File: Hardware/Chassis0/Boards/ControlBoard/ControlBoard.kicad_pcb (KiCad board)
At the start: 6 copper layers, 297.5 x 60 mm, 138 parts, among them IC3 MAX22530AWE+, IC4 MAX22530AWE+, J1 TBP02R2W-381-06BE, J11 Conn_02x10_Counter_Clockwise, J12 Conn_02x10_Counter_Clockwise, J13 Conn_02x10_Counter_Clockwise, J14 Conn_02x10_Counter_Clockwise, J2 TBP02R2W-381-06BE, J29 Conn_01x02_Pin, J3 TBP01R2W-508-02BE, J4 TBP01R1-508-04BE, J5 Conn_02x10_Counter_Clockwise, J7 TBP02R2W-381-08BE, J8 TBP02R2W-381-08BE

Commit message: Update size 0 cad model
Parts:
- removed G***: LOGO, InverterCom:HIGHVOLTAGE_20mm
- removed J11, J12, J13, J14: Conn_02x10_Counter_Clockwise, Connector_PinSocket_2.54mm:PinSocket_2x10_P2.54mm_Vertical
- removed J4: TBP01R1-508-04BE, InverterCom:TBP01R150804BE
- added C1: 100nF, Capacitor_SMD:C_1210_3225Metric_Pad1.33x2.70mm_HandSolder, F.Cu at (14.9, -37.0)
- added C10: 100nF, Capacitor_SMD:C_1210_3225Metric_Pad1.33x2.70mm_HandSolder, F.Cu at (27.0, -32.8)
- added C100: 100nF, Capacitor_SMD:C_1210_3225Metric_Pad1.33x2.70mm_HandSolder, F.Cu at (-106.3, 55.9)
- added C101: 10uF, Capacitor_SMD:C_1210_3225Metric_Pad1.33x2.70mm_HandSolder, F.Cu at (-100.3, 43.1)
- added C102: 10uF, Capacitor_SMD:C_1210_3225Metric_Pad1.33x2.70mm_HandSolder, F.Cu at (-100.3, 47.4)
- added C103: 100nF, Capacitor_SMD:C_1210_3225Metric_Pad1.33x2.70mm_HandSolder, F.Cu at (-100.3, 51.6)
- added C104: 10uF, Capacitor_SMD:C_1210_3225Metric_Pad1.33x2.70mm_HandSolder, F.Cu at (-100.3, 55.9)
- added C105: 10uF, Capacitor_SMD:C_1210_3225Metric_Pad1.33x2.70mm_HandSolder, F.Cu at (-94.3, 43.1)
- added C106: 100nF, Capacitor_SMD:C_1210_3225Metric_Pad1.33x2.70mm_HandSolder, F.Cu at (-94.3, 47.4)
- added C107: 10uF, Capacitor_SMD:C_1210_3225Metric_Pad1.33x2.70mm_HandSolder, F.Cu at (-94.3, 51.6)
- added C108: 10nF, Capacitor_SMD:C_1210_3225Metric_Pad1.33x2.70mm_HandSolder, F.Cu at (-80.3, 74.7)
- added C109: 10nF, Capacitor_SMD:C_1210_3225Metric_Pad1.33x2.70mm_HandSolder, F.Cu at (-66.2, 74.7)
- added C11: 1uF, Capacitor_SMD:C_1210_3225Metric_Pad1.33x2.70mm_HandSolder, F.Cu at (27.0, -28.5)
- added C110: 10nF, Capacitor_SMD:C_1210_3225Metric_Pad1.33x2.70mm_HandSolder, F.Cu at (-80.3, 47.5)
- added C111: 10nF, Capacitor_SMD:C_1210_3225Metric_Pad1.33x2.70mm_HandSolder, F.Cu at (-66.2, 47.5)
- added C12: 1uF, Capacitor_SMD:C_1210_3225Metric_Pad1.33x2.70mm_HandSolder, F.Cu at (27.0, -24.2)
- added C124: 10nF, Capacitor_SMD:C_1210_3225Metric_Pad1.33x2.70mm_HandSolder, F.Cu at (-107.3, 88.4)
- added C125: 10nF, Capacitor_SMD:C_1210_3225Metric_Pad1.33x2.70mm_HandSolder, F.Cu at (-148.5, 88.4)
- added C126: 10uF, Capacitor_SMD:C_1210_3225Metric_Pad1.33x2.70mm_HandSolder, F.Cu at (-24.4, -63.2)
- added C127: 10uF, Capacitor_SMD:C_1210_3225Metric_Pad1.33x2.70mm_HandSolder, F.Cu at (-135.4, 14.9)
- added C128: 10uF, Capacitor_SMD:C_1210_3225Metric_Pad1.33x2.70mm_HandSolder, F.Cu at (-53.1, 14.9)
- added C129: 10uF, Capacitor_SMD:C_1210_3225Metric_Pad1.33x2.70mm_HandSolder, F.Cu at (-94.3, 14.9)
- added C130: 10uF, Capacitor_SMD:C_1210_3225Metric_Pad1.33x2.70mm_HandSolder, F.Cu at (-135.4, 55.9)
- added C131: 10uF, Capacitor_SMD:C_1210_3225Metric_Pad1.33x2.70mm_HandSolder, F.Cu at (-94.3, 55.9)
- added C134: 10nF, Capacitor_SMD:C_1210_3225Metric_Pad1.33x2.70mm_HandSolder, F.Cu at (-162.7, 88.4)
- added C135: 10nF, Capacitor_SMD:C_1210_3225Metric_Pad1.33x2.70mm_HandSolder, F.Cu at (-121.5, 88.4)
- added C182: UCM1H101MCL1GS, InverterCom:CAPAE660X800N, F.Cu at (-113.5, 74.3)
- added C183: UCM1H101MCL1GS, InverterCom:CAPAE660X800N, F.Cu at (-43.7, -44.8)
- added C184: UCM1H101MCL1GS, InverterCom:CAPAE660X800N, F.Cu at (-154.7, 74.3)
- added C185: UCM1H101MCL1GS, InverterCom:CAPAE660X800N, F.Cu at (-113.5, 33.3)
- added C186: UCM1H101MCL1GS, InverterCom:CAPAE660X800N, F.Cu at (-72.4, 33.3)
- added C187: UCM1H101MCL1GS, InverterCom:CAPAE660X800N, F.Cu at (-154.7, 33.3)
- added C2: 1uF, Capacitor_SMD:C_1210_3225Metric_Pad1.33x2.70mm_HandSolder, F.Cu at (14.9, -32.8)
- added C25: 100nF, Capacitor_SMD:C_1210_3225Metric_Pad1.33x2.70mm_HandSolder, F.Cu at (54.5, -86.3)
- added C26: 22pF, Capacitor_SMD:C_1210_3225Metric_Pad1.33x2.70mm_HandSolder, F.Cu at (54.5, -82.0)
- added C27: 10uF, Capacitor_SMD:C_1210_3225Metric_Pad1.33x2.70mm_HandSolder, F.Cu at (-45.1, 13.0)
- added C28: 10uF, Capacitor_SMD:C_1210_3225Metric_Pad1.33x2.70mm_HandSolder, F.Cu at (-45.1, 17.3)
- added C29: 10uF, Capacitor_SMD:C_1210_3225Metric_Pad1.33x2.70mm_HandSolder, F.Cu at (-45.1, 21.5)
- added C3: 100nF, Capacitor_SMD:C_1210_3225Metric_Pad1.33x2.70mm_HandSolder, F.Cu at (14.9, -28.5)
- added C30: 22pF, Capacitor_SMD:C_1210_3225Metric_Pad1.33x2.70mm_HandSolder, F.Cu at (-45.1, 25.8)
- added C31: 100nF, Capacitor_SMD:C_1210_3225Metric_Pad1.33x2.70mm_HandSolder, F.Cu at (-39.1, 13.0)
- added C32: 100nF, Capacitor_SMD:C_1210_3225Metric_Pad1.33x2.70mm_HandSolder, F.Cu at (-39.1, 17.3)
- added C33: 10uF, Capacitor_SMD:C_1210_3225Metric_Pad1.33x2.70mm_HandSolder, F.Cu at (-39.1, 21.5)
- added C34: 100nF, Capacitor_SMD:C_1210_3225Metric_Pad1.33x2.70mm_HandSolder, F.Cu at (-39.1, 25.8)
- added C35: 22pF, Capacitor_SMD:C_1210_3225Metric_Pad1.33x2.70mm_HandSolder, F.Cu at (-33.1, 13.0)
- added C36: 22pF, Capacitor_SMD:C_1210_3225Metric_Pad1.33x2.70mm_HandSolder, F.Cu at (-33.1, 17.3)
- added C37: 22pF, Capacitor_SMD:C_1210_3225Metric_Pad1.33x2.70mm_HandSolder, F.Cu at (-33.1, 21.5)
- added C38: 100nF, Capacitor_SMD:C_1210_3225Metric_Pad1.33x2.70mm_HandSolder, F.Cu at (-36.4, -75.9)
- added C39: 10uF, Capacitor_SMD:C_1210_3225Metric_Pad1.33x2.70mm_HandSolder, F.Cu at (-36.4, -71.7)
- added C4: 1uF, Capacitor_SMD:C_1210_3225Metric_Pad1.33x2.70mm_HandSolder, F.Cu at (14.9, -24.2)
- added C40: 100nF, Capacitor_SMD:C_1210_3225Metric_Pad1.33x2.70mm_HandSolder, F.Cu at (-36.4, -67.4)
- added C41: 100nF, Capacitor_SMD:C_1210_3225Metric_Pad1.33x2.70mm_HandSolder, F.Cu at (-36.4, -63.2)
- added C42: 10uF, Capacitor_SMD:C_1210_3225Metric_Pad1.33x2.70mm_HandSolder, F.Cu at (-30.4, -75.9)
- added C43: 10uF, Capacitor_SMD:C_1210_3225Metric_Pad1.33x2.70mm_HandSolder, F.Cu at (-30.4, -71.7)
- added C44: 100nF, Capacitor_SMD:C_1210_3225Metric_Pad1.33x2.70mm_HandSolder, F.Cu at (-30.4, -67.4)
- added C45: 10uF, Capacitor_SMD:C_1210_3225Metric_Pad1.33x2.70mm_HandSolder, F.Cu at (-30.4, -63.2)
- added C46: 10uF, Capacitor_SMD:C_1210_3225Metric_Pad1.33x2.70mm_HandSolder, F.Cu at (-24.4, -75.9)
- added C47: 100nF, Capacitor_SMD:C_1210_3225Metric_Pad1.33x2.70mm_HandSolder, F.Cu at (-24.4, -71.7)
- added C48: 10uF, Capacitor_SMD:C_1210_3225Metric_Pad1.33x2.70mm_HandSolder, F.Cu at (-24.4, -67.4)
- added C5: 100nF, Capacitor_SMD:C_1210_3225Metric_Pad1.33x2.70mm_HandSolder, F.Cu at (21.0, -37.0)
- added C53: 100nF, Capacitor_SMD:C_1210_3225Metric_Pad1.33x2.70mm_HandSolder, F.Cu at (-147.5, 2.19)
- added C54: 10uF, Capacitor_SMD:C_1210_3225Metric_Pad1.33x2.70mm_HandSolder, F.Cu at (-147.5, 6.44)
- added C55: 100nF, Capacitor_SMD:C_1210_3225Metric_Pad1.33x2.70mm_HandSolder, F.Cu at (-147.5, 10.7)
- added C56: 100nF, Capacitor_SMD:C_1210_3225Metric_Pad1.33x2.70mm_HandSolder, F.Cu at (-147.5, 14.9)
- added C57: 10uF, Capacitor_SMD:C_1210_3225Metric_Pad1.33x2.70mm_HandSolder, F.Cu at (-141.5, 2.19)
- added C58: 10uF, Capacitor_SMD:C_1210_3225Metric_Pad1.33x2.70mm_HandSolder, F.Cu at (-141.5, 6.44)
- added C59: 100nF, Capacitor_SMD:C_1210_3225Metric_Pad1.33x2.70mm_HandSolder, F.Cu at (-141.5, 10.7)
- added C6: 100nF, Capacitor_SMD:C_1210_3225Metric_Pad1.33x2.70mm_HandSolder, F.Cu at (21.0, -32.8)
- added C60: 10uF, Capacitor_SMD:C_1210_3225Metric_Pad1.33x2.70mm_HandSolder, F.Cu at (-141.5, 14.9)
- added C61: 10uF, Capacitor_SMD:C_1210_3225Metric_Pad1.33x2.70mm_HandSolder, F.Cu at (-135.4, 2.19)
- added C62: 100nF, Capacitor_SMD:C_1210_3225Metric_Pad1.33x2.70mm_HandSolder, F.Cu at (-135.4, 6.44)
- added C63: 10uF, Capacitor_SMD:C_1210_3225Metric_Pad1.33x2.70mm_HandSolder, F.Cu at (-135.4, 10.7)
- added C64: 100nF, Capacitor_SMD:C_1210_3225Metric_Pad1.33x2.70mm_HandSolder, F.Cu at (-65.1, 2.19)
- added C65: 10uF, Capacitor_SMD:C_1210_3225Metric_Pad1.33x2.70mm_HandSolder, F.Cu at (-65.1, 6.44)
- added C66: 100nF, Capacitor_SMD:C_1210_3225Metric_Pad1.33x2.70mm_HandSolder, F.Cu at (-65.1, 10.7)
- added C67: 100nF, Capacitor_SMD:C_1210_3225Metric_Pad1.33x2.70mm_HandSolder, F.Cu at (-65.1, 14.9)
- added C68: 10uF, Capacitor_SMD:C_1210_3225Metric_Pad1.33x2.70mm_HandSolder, F.Cu at (-59.1, 2.19)
- added C69: 10uF, Capacitor_SMD:C_1210_3225Metric_Pad1.33x2.70mm_HandSolder, F.Cu at (-59.1, 6.44)
- added C7: 1uF, Capacitor_SMD:C_1210_3225Metric_Pad1.33x2.70mm_HandSolder, F.Cu at (21.0, -28.5)
- added C70: 100nF, Capacitor_SMD:C_1210_3225Metric_Pad1.33x2.70mm_HandSolder, F.Cu at (-59.1, 10.7)
- added C71: 10uF, Capacitor_SMD:C_1210_3225Metric_Pad1.33x2.70mm_HandSolder, F.Cu at (-59.1, 14.9)
- added C72: 10uF, Capacitor_SMD:C_1210_3225Metric_Pad1.33x2.70mm_HandSolder, F.Cu at (-53.1, 2.19)
- added C73: 100nF, Capacitor_SMD:C_1210_3225Metric_Pad1.33x2.70mm_HandSolder, F.Cu at (-53.1, 6.44)
- added C74: 10uF, Capacitor_SMD:C_1210_3225Metric_Pad1.33x2.70mm_HandSolder, F.Cu at (-53.1, 10.7)
- added C75: 100nF, Capacitor_SMD:C_1210_3225Metric_Pad1.33x2.70mm_HandSolder, F.Cu at (-106.3, 2.19)
- added C76: 10uF, Capacitor_SMD:C_1210_3225Metric_Pad1.33x2.70mm_HandSolder, F.Cu at (-106.3, 6.44)
- added C77: 100nF, Capacitor_SMD:C_1210_3225Metric_Pad1.33x2.70mm_HandSolder, F.Cu at (-106.3, 10.7)
- added C78: 100nF, Capacitor_SMD:C_1210_3225Metric_Pad1.33x2.70mm_HandSolder, F.Cu at (-106.3, 14.9)
- added C79: 10uF, Capacitor_SMD:C_1210_3225Metric_Pad1.33x2.70mm_HandSolder, F.Cu at (-100.3, 2.19)
- added C8: 1uF, Capacitor_SMD:C_1210_3225Metric_Pad1.33x2.70mm_HandSolder, F.Cu at (21.0, -24.2)
- added C80: 10uF, Capacitor_SMD:C_1210_3225Metric_Pad1.33x2.70mm_HandSolder, F.Cu at (-100.3, 6.44)
- added C81: 100nF, Capacitor_SMD:C_1210_3225Metric_Pad1.33x2.70mm_HandSolder, F.Cu at (-100.3, 10.7)
- added C82: 10uF, Capacitor_SMD:C_1210_3225Metric_Pad1.33x2.70mm_HandSolder, F.Cu at (-100.3, 14.9)
- added C83: 10uF, Capacitor_SMD:C_1210_3225Metric_Pad1.33x2.70mm_HandSolder, F.Cu at (-94.3, 2.19)
- added C84: 100nF, Capacitor_SMD:C_1210_3225Metric_Pad1.33x2.70mm_HandSolder, F.Cu at (-94.3, 6.44)
- added C85: 10uF, Capacitor_SMD:C_1210_3225Metric_Pad1.33x2.70mm_HandSolder, F.Cu at (-94.3, 10.7)
- added C86: 100nF, Capacitor_SMD:C_1210_3225Metric_Pad1.33x2.70mm_HandSolder, F.Cu at (-147.5, 43.1)
- added C87: 10uF, Capacitor_SMD:C_1210_3225Metric_Pad1.33x2.70mm_HandSolder, F.Cu at (-147.5, 47.4)
- added C88: 100nF, Capacitor_SMD:C_1210_3225Metric_Pad1.33x2.70mm_HandSolder, F.Cu at (-147.5, 51.6)
- added C89: 100nF, Capacitor_SMD:C_1210_3225Metric_Pad1.33x2.70mm_HandSolder, F.Cu at (-147.5, 55.9)
- added C9: 100nF, Capacitor_SMD:C_1210_3225Metric_Pad1.33x2.70mm_HandSolder, F.Cu at (27.0, -37.0)
- added C90: 10uF, Capacitor_SMD:C_1210_3225Metric_Pad1.33x2.70mm_HandSolder, F.Cu at (-141.5, 43.1)
- added C91: 10uF, Capacitor_SMD:C_1210_3225Metric_Pad1.33x2.70mm_HandSolder, F.Cu at (-141.5, 47.4)
- added C92: 100nF, Capacitor_SMD:C_1210_3225Metric_Pad1.33x2.70mm_HandSolder, F.Cu at (-141.5, 51.6)
- added C93: 10uF, Capacitor_SMD:C_1210_3225Metric_Pad1.33x2.70mm_HandSolder, F.Cu at (-141.5, 55.9)
- added C94: 10uF, Capacitor_SMD:C_1210_3225Metric_Pad1.33x2.70mm_HandSolder, F.Cu at (-135.4, 43.1)
- added C95: 100nF, Capacitor_SMD:C_1210_3225Metric_Pad1.33x2.70mm_HandSolder, F.Cu at (-135.4, 47.4)
- added C96: 10uF, Capacitor_SMD:C_1210_3225Metric_Pad1.33x2.70mm_HandSolder, F.Cu at (-135.4, 51.6)
- added C97: 100nF, Capacitor_SMD:C_1210_3225Metric_Pad1.33x2.70mm_HandSolder, F.Cu at (-106.3, 43.1)
- added C98: 10uF, Capacitor_SMD:C_1210_3225Metric_Pad1.33x2.70mm_HandSolder, F.Cu at (-106.3, 47.4)
- added C99: 100nF, Capacitor_SMD:C_1210_3225Metric_Pad1.33x2.70mm_HandSolder, F.Cu at (-106.3, 51.6)
- added D1: BAT54WS-7-F, InverterCom:SOD2513X120N, F.Cu at (-27.8, -54.7)
- added D10: BAT54WS-7-F, InverterCom:SOD2513X120N, F.Cu at (-138.8, 64.3)
- added D11: FM2000GP-TP, InverterCom:DIOM5226X244N, F.Cu at (-137.5, 60.8)
- added D12: BAT54WS-7-F, InverterCom:SOD2513X120N, F.Cu at (-97.7, 64.3)
- added D13: FM2000GP-TP, InverterCom:DIOM5226X244N, F.Cu at (-96.3, 60.8)
- added D14: FM2000GP-TP, InverterCom:DIOM5226X244N, F.Cu at (-137.5, 19.8)
- added D2: FM2000GP-TP, InverterCom:DIOM5226X244N, F.Cu at (-26.5, -58.3)
- added D5: BAT54WS-7-F, InverterCom:SOD2513X120N, F.Cu at (-138.8, 23.4)
- added D6: BAT54WS-7-F, InverterCom:SOD2513X120N, F.Cu at (-56.5, 23.4)
- added D7: FM2000GP-TP, InverterCom:DIOM5226X244N, F.Cu at (-55.2, 19.8)
- added D8: BAT54WS-7-F, InverterCom:SOD2513X120N, F.Cu at (-97.7, 23.4)
- added D9: FM2000GP-TP, InverterCom:DIOM5226X244N, F.Cu at (-96.3, 19.8)
- added FB1: FBMJ1608HS220NTR, InverterCom:BEADC1608X100N, F.Cu at (-28.2, -51.8)
- added FB2: FBMJ1608HS220NTR, InverterCom:BEADC1608X100N, F.Cu at (-139.3, 26.4)
- added FB3: FBMJ1608HS220NTR, InverterCom:BEADC1608X100N, F.Cu at (-56.9, 26.4)
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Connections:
- net /+5V_V renamed /+5V_C
- net /GND_V renamed /GND_C
- net /PH_U_H renamed /Control/PH_U_H_A
- net /PH_U_L renamed /Control/PH_U_L_A
- net /PH_V_H renamed /Control/PH_V_H_A
- net /PH_V_L renamed /Control/PH_V_L_A
- net /PH_W_H renamed /Control/PH_W_H_A
- net /PH_W_L renamed /Control/PH_W_L_A
- A1 pad 10: /RELAY_3_A -> unconnected-(A1-GPIO7-Pad10)
- A1 pad 11: /READY -> /Control/GATE_DRIVER_READY_A
- A1 pad 12: /RESET -> /Control/GATE_DRIVER_RESET_A
- A1 pad 31: /FAULT -> /Control/GATE_DRIVER_FAULT_A
- A1 pad 7: /RELAY_1_A -> unconnected-(A1-GPIO5-Pad7)
- A1 pad 9: /RELAY_2_A -> unconnected-(A1-GPIO6-Pad9)
- J5 pad 1: /RELAY3_NO -> unconnected-(J5-Pin_1-Pad1)
- J5 pad 12: /RELAY1_COM -> /PH_U_H_G
- J5 pad 14: unconnected-(J5-Pin_14-Pad14) -> /PH_U_H_S
- J5 pad 16: unconnected-(J5-Pin_16-Pad16) -> /DC_LINK_VSENSE_U
- J5 pad 2: unconnected-(J5-Pin_2-Pad2) -> /PH_U_L_G
- J5 pad 4: /RELAY3_COM -> /GND_U
- J5 pad 5: /RELAY2_NO -> unconnected-(J5-Pin_5-Pad5)
- J5 pad 6: unconnected-(J5-Pin_6-Pad6) -> /PH_U_L_D
- J5 pad 8: /RELAY2_COM -> unconnected-(J5-Pin_8-Pad8)
- J5 pad 9: /RELAY1_NO -> unconnected-(J5-Pin_9-Pad9)
- J7 pad 1: /CAN_JUMPER_B -> /CAN/CAN_GND
- J7 pad 2: /CAN_JUMPER_A -> /CAN/CAN_H_B
- J7 pad 3: unconnected-(J7-Pad3) -> /CAN/CAN_L_B
- J7 pad 4: /CAN_24V_OUT -> /CAN/CAN_H_B
- J7 pad 5: unconnected-(J7-Pad5) -> /CAN/CAN_JMP_B
- J7 pad 6: /CAN_LOW -> unconnected-(J7-Pad6)
- J7 pad 7: /CAN_HIGH -> unconnected-(J7-Pad7)
- J7 pad 8: /CAN_GND -> unconnected-(J7-Pad8)
- J8 pad 2: unconnected-(J8-Pad2) -> /PH_W_L_G
- J8 pad 3: /RELAY3_NO -> unconnected-(J8-Pin_3-Pad3)
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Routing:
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- removed copper zone on In3.Cu, net /+12V_A
- removed copper zone on In2.Cu, net /+3.3V_A
- removed copper zone on In2.Cu, net /+5V_C
- removed copper zone on In2.Cu, net /+5V_W
- removed copper zone on B.Cu, net /CAN_GND
- removed copper zone on F.Cu, net /CAN_GND
- removed copper zone on In1.Cu, net /CAN_GND
- removed copper zone on In4.Cu, net /CAN_GND
- removed copper zone on B.Cu, net /GND_A
- removed copper zone on F.Cu, net /GND_A
- removed copper zone on In1.Cu, net /GND_A
- removed copper zone on In4.Cu, net /GND_A
- removed copper zone on B.Cu, net /GND_C
- removed copper zone on F.Cu, net /GND_C
- removed copper zone on In1.Cu, net /GND_C
- removed copper zone on In4.Cu, net /GND_C
- removed copper zone on B.Cu, net /GND_W
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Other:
- board size 297.5 x 60 mm -> 200 x 110 mm
- board text added: "OPTIONS: - EITHER, CREATE SEPARATE GATE DRIVER BOARD AND USE THAT TO FREE UP SPACE OR - EXPAND BOARD OUTLINE MORE, TO MAKE IT ALL FIT OR - CUT OUT FEATURES - REMOVE THROTTLE ADC (THEN EITHER NO TEMP SENSE FOR MOSFETS, OR REMOVE ONE PHASE AND TIE IT THERE INSTEAD) - REMOVE REMOVE VOLTAGE SENSE ADC (BUT THEN NO DC BUS VOLTAGE SENSE) - NOT IDEAL"
- board text removed: "+5V H_U H_W H_V MTRTMP GND"
- board text removed: "+5V NC RGN SPRE THRT GND"
- board text removed: "1->"
- board text removed: "<-1"
- board text removed: "C2-CTRL-XX12 REVISION A"
- board text removed: "DANGER! HAZARDOUS VOLTAGES PRESENT REMOVE POWER AND VERIFY CAPACITORS DISCHARGED BEFORE SERVICING"
- board text removed: "DESIGNED BY THOMAS LIAO"
- board text removed: "GND CH CL NC +24v NC CJPA CJPB"
- board text removed: "GND VIN (10-16V)"
- board text removed: "ISOLATION BARRIER"
- board text removed: "ISOLATION BARRIER DO NOT CROSS"
- board text removed: "NC GND HS_TMP +5V"
- board text removed: "R1NO R1COM R2COM R2NO R3COM R3NO NC NC"
- board text removed: "SERIAL NUMBER"
- board text removed: "[ ] 12VIN NOM [ ] 15VIN NOM [ ] 24VIN NOM [ ] 48VIN NOM"

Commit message: Add control board outline for size 0
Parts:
- removed C1, C10, C100, C103, C106, C13, C132, C14, C17, C18, C19, C20, C25, C3, C31, C32, C34, C38, C40, C41, C44, C47, C5, C50, C52, C53, C55, C56, C59, C6, C62, C64, C66, C67, C70, C73, C75, C77, C78, C81, C84, C86, C88, C89, C9, C92, C95, C97, C99: 100nF, Capacitor_SMD:C_1210_3225Metric_Pad1.33x2.70mm_HandSolder
- removed C101, C102, C104, C105, C107, C126, C127, C128, C129, C130, C131, C133, C27, C28, C29, C33, C39, C42, C43, C45, C46, C48, C54, C57, C58, C60, C61, C63, C65, C68, C69, C71, C72, C74, C76, C79, C80, C82, C83, C85, C87, C90, C91, C93, C94, C96, C98: 10uF, Capacitor_SMD:C_1210_3225Metric_Pad1.33x2.70mm_HandSolder
- removed C108, C109, C110, C111, C116, C117, C118, C119, C120, C121, C122, C123, C124, C125, C134, C135: 10nF, Capacitor_SMD:C_1210_3225Metric_Pad1.33x2.70mm_HandSolder
- removed C11, C12, C15, C16, C2, C21, C23, C4, C49, C51, C7, C8: 1uF, Capacitor_SMD:C_1210_3225Metric_Pad1.33x2.70mm_HandSolder
- removed C140, C141, C142, C143, C144, C145, C146, C147, C148, C149, C150, C151, C152, C153, C154, C155, C156, C157, C158, C159, C160, C161, C162, C163, C164, C165, C166, C167, C168, C169, C170, C171, C172, C173, C174, C175, C176, C177, C178, C179, C180, C181, C182, C183, C184, C185, C186, C187: UCM1H101MCL1GS, InverterCom:CAPAE660X800N
- removed C26, C30, C35, C36, C37: 22pF, Capacitor_SMD:C_1210_3225Metric_Pad1.33x2.70mm_HandSolder
- removed D1, D10, D12, D5, D6, D8: BAT54WS-7-F, InverterCom:SOD2513X120N
- removed D11, D13, D14, D2, D7, D9: FM2000GP-TP, InverterCom:DIOM5226X244N
- removed D3, D4: S3N, InverterCom:DIOM8059X265N
- removed F1: MF-RHT200_32-2, InverterCom:MFRHT200322
- removed FB1, FB2, FB3, FB4, FB5, FB6: FBMJ1608HS220NTR, InverterCom:BEADC1608X100N
- removed FL1: ACT45B-101-2P-TL003, InverterCom:ACT45B1012PTL003
- removed H5: MountingHole, MountingHole:MountingHole_4.3mm_M4
- removed H7: MountingHole, MountingHole:MountingHole_3.2mm_M3
- removed IC10, IC11, IC12, IC7, IC8, IC9: ADUM4136BRWZ, InverterCom:SOIC127P1032X265-16N
- removed IC5: MCP2515-e_ST, InverterCom:SOP65P640X120-20N
- removed IC6: ISO1042BDWVR, InverterCom:SOIC127P1150X280-8N
- removed J29: Conn_01x02_Pin, Connector_PinHeader_2.54mm:PinHeader_1x02_P2.54mm_Vertical
- removed J7: TBP02R2W-381-08BE, InverterCom:TBP02R2W38108BE
- removed LED1, LED10, LED13, LED16, LED17, LED20, LED21, LED24, LED25, LED28, LED29, LED32, LED35, LED5, LED7: LTST-C230GKT, InverterCom:LEDC3216X120N
- removed LED14, LED15, LED18, LED19, LED2, LED22, LED23, LED26, LED27, LED3, LED30, LED31, LED4, LED6, LED8, LED9: LTST-C230CKT, InverterCom:LEDC3216X120N
- removed PS10, PS11, PS12, PS5, PS8, PS9: MGJ2D121509MPC-R7, InverterCom:MGJ2D121509MPCR7
- removed PS2, PS3, PS4, PS7: RKE-1205S_H, InverterCom:RKE1205SH
- removed R1, R14, R2, R22, R23, R25, R3, R33, R34, R35, R43, R44, R45, R53, R54, R55, R63, R64, R65, R73, R74, R8: 4.7k, Resistor_SMD:R_1210_3225Metric_Pad1.30x2.65mm_HandSolder
- removed R10, R11, R125, R15, R26, R36, R4, R46, R56, R66: 220, Resistor_SMD:R_1210_3225Metric_Pad1.30x2.65mm_HandSolder
- removed R107, R109, R111, R113, R115, R117, R119, R121, R123, R124, R126, R127, R19, R20, R30, R31, R40, R41, R5, R50, R51, R6, R60, R61, R7, R70, R71, R76, R82, R88, R94: 1k, Resistor_SMD:R_1210_3225Metric_Pad1.30x2.65mm_HandSolder
- removed R108, R110, R112, R114, R116, R118, R120, R122, R128, R129, R130, R131: 5k, Resistor_SMD:R_1210_3225Metric_Pad1.30x2.65mm_HandSolder
- removed R12, R16, R21, R27, R32, R37, R42, R47, R52, R57, R62, R67, R72: 0, Resistor_SMD:R_1210_3225Metric_Pad1.30x2.65mm_HandSolder
- removed R13: 10k, Resistor_SMD:R_1210_3225Metric_Pad1.30x2.65mm_HandSolder
- removed R17, R28, R38, R48, R58, R68: 9.1, Resistor_SMD:R_1210_3225Metric_Pad1.30x2.65mm_HandSolder
- removed R18, R29, R39, R49, R59, R69: 6.8, Resistor_SMD:R_1210_3225Metric_Pad1.30x2.65mm_HandSolder
- removed R75, R81, R87, R93: 2k, Resistor_SMD:R_1210_3225Metric_Pad1.30x2.65mm_HandSolder
- removed R77, R78, R79, R80, R83, R84, R85, R86, R89, R90, R91, R92, R95, R96, R97, R98: 250k, Resistor_SMD:R_1210_3225Metric_Pad1.30x2.65mm_HandSolder
- removed R9: 120, Resistor_SMD:R_1210_3225Metric_Pad1.30x2.65mm_HandSolder
- removed TP1, TP10, TP11, TP12, TP2, TP21, TP22, TP23, TP24, TP29, TP3, TP30, TP31, TP32, TP33, TP34, TP35, TP36, TP37, TP38, TP39, TP4, TP5, TP6, TP7, TP8, TP9: TestPoint, TestPoint:TestPoint_Loop_D2.54mm_Drill1.5mm_Beaded
- removed Y1: 8MHz, Crystal:Crystal_HC49-4H_Vertical
- removed Z1, Z10, Z11, Z12, Z13, Z14, Z15, Z16, Z17, Z18, Z19, Z2, Z20, Z3, Z4, Z9: SZMMSZ4678T1G, InverterCom:SOD3716X135N
- added J10: Conn_02x08_Counter_Clockwise, Connector_PinSocket_2.54mm:PinSocket_2x08_P2.54mm_Vertical, F.Cu at (7.42, 62.5)
- moved IC2 125.7 mm to (29.4, 85.3)
- moved IC4 37.7 mm to (150.0, 50.0), turned to 180 degrees
- moved IC1 35.0 mm to (135.0, 80.0)
- moved J1 32.0 mm to (175.0, 74.0)
- moved IC3 31.6 mm to (150.0, 65.6), turned to 180 degrees
- moved J2 19.2 mm to (175.0, 38.8), turned to 90 degrees
- moved PS1 6.02 mm to (2.29, 58.1)
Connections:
- A1 pad 11: /Control/GATE_DRIVER_READY_A -> /READY
- A1 pad 12: /Control/GATE_DRIVER_RESET_A -> /RESET
- A1 pad 21: /Control/PH_U_L_A -> /PH_U_L
- A1 pad 22: /Control/PH_U_H_A -> /PH_U_H
- A1 pad 24: /Control/PH_V_L_A -> /PH_V_L
- A1 pad 25: /Control/PH_V_H_A -> /PH_V_H
- A1 pad 26: /Control/PH_W_L_A -> /PH_W_L
- A1 pad 27: /Control/PH_W_H_A -> /PH_W_H
- A1 pad 31: /Control/GATE_DRIVER_FAULT_A -> /FAULT
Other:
- board size 200 x 110 mm -> 180 x 110 mm
- board text removed: "OPTIONS: - EITHER, CREATE SEPARATE GATE DRIVER BOARD AND USE THAT TO FREE UP SPACE OR - EXPAND BOARD OUTLINE MORE, TO MAKE IT ALL FIT OR - CUT OUT FEATURES - REMOVE THROTTLE ADC (THEN EITHER NO TEMP SENSE FOR MOSFETS, OR REMOVE ONE PHASE AND TIE IT THERE INSTEAD) - REMOVE REMOVE VOLTAGE SENSE ADC (BUT THEN NO DC BUS VOLTAGE SENSE) - NOT IDEAL"

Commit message: finish chassis 0 board design v1
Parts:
- removed H8: MountingHole, MountingHole:MountingHole_4.3mm_M4
- added C1: 100nF, Capacitor_SMD:C_1210_3225Metric_Pad1.33x2.70mm_HandSolder, B.Cu at (130.5, 92.0)
- added C10: 100nF, Capacitor_SMD:C_1210_3225Metric_Pad1.33x2.70mm_HandSolder, F.Cu at (34.6, 94.8)
- added C108: 10nF, Capacitor_SMD:C_1210_3225Metric_Pad1.33x2.70mm_HandSolder, F.Cu at (24.0, 91.0)
- added C109: 10nF, Capacitor_SMD:C_1210_3225Metric_Pad1.33x2.70mm_HandSolder, F.Cu at (43.0, 101.5)
- added C11: 1uF, Capacitor_SMD:C_1210_3225Metric_Pad1.33x2.70mm_HandSolder, B.Cu at (44.6, 93.8)
- added C110: 10nF, Capacitor_SMD:C_1210_3225Metric_Pad1.33x2.70mm_HandSolder, F.Cu at (56.5, 98.5)
- added C111: 10nF, Capacitor_SMD:C_1210_3225Metric_Pad1.33x2.70mm_HandSolder, F.Cu at (94.5, 100.0)
- added C116: 10nF, Capacitor_SMD:C_1210_3225Metric_Pad1.33x2.70mm_HandSolder, B.Cu at (164.6, 76.5)
- added C117: 10nF, Capacitor_SMD:C_1210_3225Metric_Pad1.33x2.70mm_HandSolder, B.Cu at (164.5, 69.0)
- added C118: 10nF, Capacitor_SMD:C_1210_3225Metric_Pad1.33x2.70mm_HandSolder, B.Cu at (164.6, 60.0)
- added C119: 10nF, Capacitor_SMD:C_1210_3225Metric_Pad1.33x2.70mm_HandSolder, B.Cu at (164.6, 64.5)
- added C12: 1uF, Capacitor_SMD:C_1210_3225Metric_Pad1.33x2.70mm_HandSolder, B.Cu at (34.6, 94.8)
- added C120: 10nF, Capacitor_SMD:C_1210_3225Metric_Pad1.33x2.70mm_HandSolder, B.Cu at (165.4, 34.0)
- added C121: 10nF, Capacitor_SMD:C_1210_3225Metric_Pad1.33x2.70mm_HandSolder, B.Cu at (165.5, 20.5)
- added C122: 10nF, Capacitor_SMD:C_1210_3225Metric_Pad1.33x2.70mm_HandSolder, B.Cu at (165.4, 29.5)
- added C123: 10nF, Capacitor_SMD:C_1210_3225Metric_Pad1.33x2.70mm_HandSolder, B.Cu at (165.4, 25.0)
- added C124: 10nF, Capacitor_SMD:C_1210_3225Metric_Pad1.33x2.70mm_HandSolder, F.Cu at (168.0, 94.5)
- added C125: 10nF, Capacitor_SMD:C_1210_3225Metric_Pad1.33x2.70mm_HandSolder, B.Cu at (170.0, 94.5)
- added C13: 100nF, Capacitor_SMD:C_1210_3225Metric_Pad1.33x2.70mm_HandSolder, F.Cu at (139.5, 54.5)
- added C132: 100nF, Capacitor_SMD:C_1210_3225Metric_Pad1.33x2.70mm_HandSolder, B.Cu at (91.4, 59.5)
- added C133: 10uF, Capacitor_SMD:C_1210_3225Metric_Pad1.33x2.70mm_HandSolder, B.Cu at (91.4, 56.0)
- added C134: 10nF, Capacitor_SMD:C_1210_3225Metric_Pad1.33x2.70mm_HandSolder, B.Cu at (157.0, 94.5)
- added C135: 10nF, Capacitor_SMD:C_1210_3225Metric_Pad1.33x2.70mm_HandSolder, F.Cu at (154.5, 94.5)
- added C14: 100nF, Capacitor_SMD:C_1210_3225Metric_Pad1.33x2.70mm_HandSolder, F.Cu at (140.0, 76.0)
- added C141: UCM1H101MCL1GS, InverterCom:CAPAE660X800N, B.Cu at (8.00, 32.0)
- added C143: UCM1H101MCL1GS, InverterCom:CAPAE660X800N, B.Cu at (16.5, 24.0)
- added C144: UCM1H101MCL1GS, InverterCom:CAPAE660X800N, F.Cu at (13.9, 74.5)
- added C145: UCM1H101MCL1GS, InverterCom:CAPAE660X800N, F.Cu at (21.7, 74.5)
- added C146: UCM1H101MCL1GS, InverterCom:CAPAE660X800N, F.Cu at (29.5, 74.5)
- added C147: UCM1H101MCL1GS, InverterCom:CAPAE660X800N, F.Cu at (5.70, 74.5)
- added C148: UCM1H101MCL1GS, InverterCom:CAPAE660X800N, B.Cu at (56.0, 84.0)
- added C149: UCM1H101MCL1GS, InverterCom:CAPAE660X800N, F.Cu at (56.0, 84.0)
- added C15: 1uF, Capacitor_SMD:C_1210_3225Metric_Pad1.33x2.70mm_HandSolder, F.Cu at (135.0, 54.5)
- added C150: UCM1H101MCL1GS, InverterCom:CAPAE660X800N, F.Cu at (121.0, 61.5)
- added C151: UCM1H101MCL1GS, InverterCom:CAPAE660X800N, F.Cu at (121.0, 71.8)
- added C16: 1uF, Capacitor_SMD:C_1210_3225Metric_Pad1.33x2.70mm_HandSolder, F.Cu at (136.5, 76.0)
- added C17: 100nF, Capacitor_SMD:C_1210_3225Metric_Pad1.33x2.70mm_HandSolder, F.Cu at (149.5, 55.4)
- added C18: 100nF, Capacitor_SMD:C_1210_3225Metric_Pad1.33x2.70mm_HandSolder, B.Cu at (153.8, 46.9)
- added C19: 100nF, Capacitor_SMD:C_1210_3225Metric_Pad1.33x2.70mm_HandSolder, F.Cu at (149.5, 76.5)
- added C2: 1uF, Capacitor_SMD:C_1210_3225Metric_Pad1.33x2.70mm_HandSolder, B.Cu at (127.0, 92.0)
- added C20: 100nF, Capacitor_SMD:C_1210_3225Metric_Pad1.33x2.70mm_HandSolder, B.Cu at (153.5, 68.1)
- added C21: 1uF, Capacitor_SMD:C_1210_3225Metric_Pad1.33x2.70mm_HandSolder, F.Cu at (153.0, 55.6)
- added C23: 1uF, Capacitor_SMD:C_1210_3225Metric_Pad1.33x2.70mm_HandSolder, F.Cu at (153.0, 76.5)
- added C25: 100nF, Capacitor_SMD:C_1210_3225Metric_Pad1.33x2.70mm_HandSolder, F.Cu at (70.5, 86.0)
- added C26: 22pF, Capacitor_SMD:C_1210_3225Metric_Pad1.33x2.70mm_HandSolder, B.Cu at (71.4, 74.5)
- added C27: 10uF, Capacitor_SMD:C_1210_3225Metric_Pad1.33x2.70mm_HandSolder, B.Cu at (75.0, 87.0)
- added C28: 10uF, Capacitor_SMD:C_1210_3225Metric_Pad1.33x2.70mm_HandSolder, B.Cu at (79.1, 80.5)
- added C29: 10uF, Capacitor_SMD:C_1210_3225Metric_Pad1.33x2.70mm_HandSolder, F.Cu at (66.0, 86.0)
- added C3: 100nF, Capacitor_SMD:C_1210_3225Metric_Pad1.33x2.70mm_HandSolder, B.Cu at (44.5, 81.0)
- added C30: 22pF, Capacitor_SMD:C_1210_3225Metric_Pad1.33x2.70mm_HandSolder, B.Cu at (83.0, 73.0)
- added C31: 100nF, Capacitor_SMD:C_1210_3225Metric_Pad1.33x2.70mm_HandSolder, B.Cu at (80.1, 89.5)
- added C32: 100nF, Capacitor_SMD:C_1210_3225Metric_Pad1.33x2.70mm_HandSolder, B.Cu at (79.0, 77.0)
- added C33: 10uF, Capacitor_SMD:C_1210_3225Metric_Pad1.33x2.70mm_HandSolder, B.Cu at (91.0, 73.5)
- added C34: 100nF, Capacitor_SMD:C_1210_3225Metric_Pad1.33x2.70mm_HandSolder, F.Cu at (91.0, 73.5)
- added C35: 22pF, Capacitor_SMD:C_1210_3225Metric_Pad1.33x2.70mm_HandSolder, F.Cu at (99.0, 73.9)
- added C36: 22pF, Capacitor_SMD:C_1210_3225Metric_Pad1.33x2.70mm_HandSolder, F.Cu at (103.6, 82.0)
- added C37: 22pF, Capacitor_SMD:C_1210_3225Metric_Pad1.33x2.70mm_HandSolder, F.Cu at (103.5, 77.5)
- added C4: 1uF, Capacitor_SMD:C_1210_3225Metric_Pad1.33x2.70mm_HandSolder, B.Cu at (44.5, 77.5)
- added C49: 1uF, Capacitor_SMD:C_1210_3225Metric_Pad1.33x2.70mm_HandSolder, B.Cu at (14.5, 34.5)
- added C5: 100nF, Capacitor_SMD:C_1210_3225Metric_Pad1.33x2.70mm_HandSolder, B.Cu at (140.2, 90.4)
- added C50: 100nF, Capacitor_SMD:C_1210_3225Metric_Pad1.33x2.70mm_HandSolder, B.Cu at (14.5, 31.0)
- added C51: 1uF, Capacitor_SMD:C_1210_3225Metric_Pad1.33x2.70mm_HandSolder, B.Cu at (10.5, 51.0)
- added C52: 100nF, Capacitor_SMD:C_1210_3225Metric_Pad1.33x2.70mm_HandSolder, B.Cu at (15.5, 51.0)
- added C6: 100nF, Capacitor_SMD:C_1210_3225Metric_Pad1.33x2.70mm_HandSolder, F.Cu at (144.7, 100.4)
- added C7: 1uF, Capacitor_SMD:C_1210_3225Metric_Pad1.33x2.70mm_HandSolder, B.Cu at (143.7, 90.4)
- added C8: 1uF, Capacitor_SMD:C_1210_3225Metric_Pad1.33x2.70mm_HandSolder, B.Cu at (144.7, 100.4)
- added C9: 100nF, Capacitor_SMD:C_1210_3225Metric_Pad1.33x2.70mm_HandSolder, F.Cu at (44.6, 93.8)
- added D3: S3N, InverterCom:DIOM8059X265N, F.Cu at (3.50, 19.0)
- added D4: S3N, InverterCom:DIOM8059X265N, B.Cu at (3.50, 19.0)
- added F1: MF-RHT200_32-2, InverterCom:MFRHT200322, F.Cu at (8.50, 11.5)
- added FL1: ACT45B-101-2P-TL003, InverterCom:ACT45B1012PTL003, F.Cu at (96.5, 79.6)
- added H2: MountingHole, MountingHole:MountingHole_4.3mm_M4, F.Cu at (175.0, 5.00)
- added H6: MountingHole, MountingHole:MountingHole_4.3mm_M4, F.Cu at (40.0, 64.0)
- added H9: MountingHole, MountingHole:MountingHole_4.3mm_M4, F.Cu at (121.0, 82.0)
- added IC5: MCP2515-e_ST, InverterCom:SOP65P640X120-20N, F.Cu at (74.1, 79.6)
- added IC6: ISO1042BDWVR, InverterCom:SOIC127P1150X280-8N, F.Cu at (85.8, 79.6)
- added J29: Conn_01x02_Pin, Connector_PinHeader_2.54mm:PinHeader_1x02_P2.54mm_Vertical, F.Cu at (108.5, 45.0)
- added J7: TBP02R2W-381-08BE, InverterCom:TBP02R2W38108BE, F.Cu at (110.0, 68.3)
- added PS2: RKE-1205S_H, InverterCom:RKE1205SH, F.Cu at (138.2, 43.1)
- added PS3: RKE-1205S_H, InverterCom:RKE1205SH, F.Cu at (137.7, 63.6)
- added PS4: RKE-1205S_H, InverterCom:RKE1205SH, F.Cu at (131.2, 83.6)
- added PS7: RKE-1205S_H, InverterCom:RKE1205SH, F.Cu at (78.8, 86.5)
- added R107: 1k, Resistor_SMD:R_1210_3225Metric_Pad1.30x2.65mm_HandSolder, F.Cu at (168.0, 76.5)
- added R108: 5k, Resistor_SMD:R_1210_3225Metric_Pad1.30x2.65mm_HandSolder, B.Cu at (171.1, 76.5)
- added R109: 1k, Resistor_SMD:R_1210_3225Metric_Pad1.30x2.65mm_HandSolder, F.Cu at (168.0, 69.0)
- added R110: 5k, Resistor_SMD:R_1210_3225Metric_Pad1.30x2.65mm_HandSolder, B.Cu at (171.1, 69.0)
- added R111: 1k, Resistor_SMD:R_1210_3225Metric_Pad1.30x2.65mm_HandSolder, F.Cu at (167.9, 60.0)
- added R112: 5k, Resistor_SMD:R_1210_3225Metric_Pad1.30x2.65mm_HandSolder, B.Cu at (170.9, 60.0)
- added R113: 1k, Resistor_SMD:R_1210_3225Metric_Pad1.30x2.65mm_HandSolder, F.Cu at (167.9, 64.5)
- added R114: 5k, Resistor_SMD:R_1210_3225Metric_Pad1.30x2.65mm_HandSolder, B.Cu at (170.9, 64.5)
- added R115: 1k, Resistor_SMD:R_1210_3225Metric_Pad1.30x2.65mm_HandSolder, F.Cu at (168.5, 34.0)
- added R116: 5k, Resistor_SMD:R_1210_3225Metric_Pad1.30x2.65mm_HandSolder, B.Cu at (171.6, 34.0)
- added R117: 1k, Resistor_SMD:R_1210_3225Metric_Pad1.30x2.65mm_HandSolder, F.Cu at (168.5, 20.5)
- added R118: 5k, Resistor_SMD:R_1210_3225Metric_Pad1.30x2.65mm_HandSolder, B.Cu at (171.6, 20.5)
- added R119: 1k, Resistor_SMD:R_1210_3225Metric_Pad1.30x2.65mm_HandSolder, F.Cu at (168.5, 29.5)
- added R120: 5k, Resistor_SMD:R_1210_3225Metric_Pad1.30x2.65mm_HandSolder, B.Cu at (171.6, 29.5)
- added R121: 1k, Resistor_SMD:R_1210_3225Metric_Pad1.30x2.65mm_HandSolder, F.Cu at (168.5, 25.0)
- added R122: 5k, Resistor_SMD:R_1210_3225Metric_Pad1.30x2.65mm_HandSolder, B.Cu at (171.5, 25.0)
- added R123: 1k, Resistor_SMD:R_1210_3225Metric_Pad1.30x2.65mm_HandSolder, B.Cu at (165.5, 94.5)
- added R124: 1k, Resistor_SMD:R_1210_3225Metric_Pad1.30x2.65mm_HandSolder, F.Cu at (150.0, 94.5)
- added R126: 1k, Resistor_SMD:R_1210_3225Metric_Pad1.30x2.65mm_HandSolder, F.Cu at (163.5, 94.5)
- added R127: 1k, Resistor_SMD:R_1210_3225Metric_Pad1.30x2.65mm_HandSolder, B.Cu at (152.5, 94.5)
- added R128: 5k, Resistor_SMD:R_1210_3225Metric_Pad1.30x2.65mm_HandSolder, B.Cu at (168.0, 100.0)
- added R129: 5k, Resistor_SMD:R_1210_3225Metric_Pad1.30x2.65mm_HandSolder, B.Cu at (157.0, 100.0)
- added R13: 10k, Resistor_SMD:R_1210_3225Metric_Pad1.30x2.65mm_HandSolder, F.Cu at (172.5, 83.5)
- added R130: 5k, Resistor_SMD:R_1210_3225Metric_Pad1.30x2.65mm_HandSolder, F.Cu at (165.5, 100.0)
- added R131: 5k, Resistor_SMD:R_1210_3225Metric_Pad1.30x2.65mm_HandSolder, F.Cu at (154.5, 100.0)
- added R75: 2k, Resistor_SMD:R_1210_3225Metric_Pad1.30x2.65mm_HandSolder, F.Cu at (19.0, 91.0)
- added R76: 1k, Resistor_SMD:R_1210_3225Metric_Pad1.30x2.65mm_HandSolder, F.Cu at (14.0, 91.0)
- added R77: 250k, Resistor_SMD:R_1210_3225Metric_Pad1.30x2.65mm_HandSolder, F.Cu at (9.50, 95.5)
- added R78: 250k, Resistor_SMD:R_1210_3225Metric_Pad1.30x2.65mm_HandSolder, F.Cu at (8.00, 91.0)
- added R79: 250k, Resistor_SMD:R_1210_3225Metric_Pad1.30x2.65mm_HandSolder, F.Cu at (2.00, 91.0)
- added R8: 4.7k, Resistor_SMD:R_1210_3225Metric_Pad1.30x2.65mm_HandSolder, F.Cu at (65.0, 81.5)
- added R80: 250k, Resistor_SMD:R_1210_3225Metric_Pad1.30x2.65mm_HandSolder, F.Cu at (2.00, 96.5)
- added R81: 2k, Resistor_SMD:R_1210_3225Metric_Pad1.30x2.65mm_HandSolder, F.Cu at (41.5, 107.0)
- added R82: 1k, Resistor_SMD:R_1210_3225Metric_Pad1.30x2.65mm_HandSolder, F.Cu at (37.0, 107.0)
- added R83: 250k, Resistor_SMD:R_1210_3225Metric_Pad1.30x2.65mm_HandSolder, F.Cu at (37.0, 101.5)
- added R84: 250k, Resistor_SMD:R_1210_3225Metric_Pad1.30x2.65mm_HandSolder, F.Cu at (31.5, 100.0)
- added R85: 250k, Resistor_SMD:R_1210_3225Metric_Pad1.30x2.65mm_HandSolder, F.Cu at (26.0, 100.0)
- added R86: 250k, Resistor_SMD:R_1210_3225Metric_Pad1.30x2.65mm_HandSolder, F.Cu at (20.5, 100.0)
- added R87: 2k, Resistor_SMD:R_1210_3225Metric_Pad1.30x2.65mm_HandSolder, F.Cu at (61.0, 98.5)
- added R88: 1k, Resistor_SMD:R_1210_3225Metric_Pad1.30x2.65mm_HandSolder, F.Cu at (52.0, 98.5)
- added R89: 250k, Resistor_SMD:R_1210_3225Metric_Pad1.30x2.65mm_HandSolder, F.Cu at (52.0, 106.0)
- added R9: 120, Resistor_SMD:R_1210_3225Metric_Pad1.30x2.65mm_HandSolder, F.Cu at (99.5, 85.0)
- added R90: 250k, Resistor_SMD:R_1210_3225Metric_Pad1.30x2.65mm_HandSolder, F.Cu at (58.0, 106.0)
- added R91: 250k, Resistor_SMD:R_1210_3225Metric_Pad1.30x2.65mm_HandSolder, F.Cu at (61.5, 106.0)
- added R92: 250k, Resistor_SMD:R_1210_3225Metric_Pad1.30x2.65mm_HandSolder, F.Cu at (67.5, 106.0)
- added R93: 2k, Resistor_SMD:R_1210_3225Metric_Pad1.30x2.65mm_HandSolder, F.Cu at (99.0, 100.0)
- added R94: 1k, Resistor_SMD:R_1210_3225Metric_Pad1.30x2.65mm_HandSolder, F.Cu at (90.0, 100.0)
- added R95: 250k, Resistor_SMD:R_1210_3225Metric_Pad1.30x2.65mm_HandSolder, F.Cu at (96.0, 106.0)
- added R96: 250k, Resistor_SMD:R_1210_3225Metric_Pad1.30x2.65mm_HandSolder, F.Cu at (102.0, 106.0)
- added R97: 250k, Resistor_SMD:R_1210_3225Metric_Pad1.30x2.65mm_HandSolder, F.Cu at (106.0, 106.0)
- added R98: 250k, Resistor_SMD:R_1210_3225Metric_Pad1.30x2.65mm_HandSolder, F.Cu at (112.0, 106.0)
- added Y1: 8MHz, Crystal:Crystal_HC49-4H_Vertical, F.Cu at (74.5, 73.0)
- added Z1: SZMMSZ4678T1G, InverterCom:SOD3716X135N, F.Cu at (27.5, 91.0)
- added Z10: SZMMSZ4678T1G, InverterCom:SOD3716X135N, F.Cu at (161.2, 69.0)
- added Z11: SZMMSZ4678T1G, InverterCom:SOD3716X135N, F.Cu at (161.3, 60.0)
- added Z12: SZMMSZ4678T1G, InverterCom:SOD3716X135N, F.Cu at (161.2, 64.5)
- added Z13: SZMMSZ4678T1G, InverterCom:SOD3716X135N, F.Cu at (163.0, 34.0)
- added Z14: SZMMSZ4678T1G, InverterCom:SOD3716X135N, F.Cu at (163.0, 20.5)
- added Z15: SZMMSZ4678T1G, InverterCom:SOD3716X135N, F.Cu at (163.0, 29.5)
- added Z16: SZMMSZ4678T1G, InverterCom:SOD3716X135N, F.Cu at (163.0, 25.0)
- added Z17: SZMMSZ4678T1G, InverterCom:SOD3716X135N, F.Cu at (171.5, 94.5)
- added Z18: SZMMSZ4678T1G, InverterCom:SOD3716X135N, B.Cu at (174.0, 94.5)
- added Z19: SZMMSZ4678T1G, InverterCom:SOD3716X135N, B.Cu at (161.0, 94.5)
- added Z2: SZMMSZ4678T1G, InverterCom:SOD3716X135N, F.Cu at (45.5, 107.0)
- added Z20: SZMMSZ4678T1G, InverterCom:SOD3716X135N, F.Cu at (159.0, 94.5)
- added Z3: SZMMSZ4678T1G, InverterCom:SOD3716X135N, F.Cu at (64.5, 98.5)
- added Z4: SZMMSZ4678T1G, InverterCom:SOD3716X135N, F.Cu at (102.5, 100.0)
- added Z9: SZMMSZ4678T1G, InverterCom:SOD3716X135N, F.Cu at (161.2, 76.5)
- H1: footprint MountingHole:MountingHole_3.2mm_M3 -> MountingHole:MountingHole_4.3mm_M4
- IC3, IC4: moved to B.Cu
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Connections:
- A1 pad 33: Net-(A1-AGND) -> /GND_A
- IC1 pad 2: /ISENSE_GND_Y -> /GND_Y
- IC1 pad 8: /ISENSE_GND_Y -> /GND_Y
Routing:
- net /SPI2_SCK_A: track 0.00 -> 195.9 mm, vias 0 -> 5
- net /SPI2_TX_A: track 0.00 -> 189.3 mm, vias 0 -> 5
- net /SPI2_RX_A: track 0.00 -> 187.5 mm, vias 0 -> 5
- net /SPI2_ADC2_CS_A: track 0.00 -> 128.0 mm, vias 0 -> 1
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- added copper zone on In2.Cu, net /+12V_A
- added copper zone on In3.Cu, net /+3.3V_A
- added copper zone on In3.Cu, net /+5V_C
- added copper zone on In3.Cu, net /+5V_W
- added copper zone on B.Cu, net /CAN/CAN_GND
- added copper zone on F.Cu, net /CAN/CAN_GND
- added copper zone on In1.Cu, net /CAN/CAN_GND
- added copper zone on In4.Cu, net /CAN/CAN_GND
- added copper zone on In2.Cu, net /CAN/CAN_ISO_5V
- added copper zone on In3.Cu, net /CAN/CAN_ISO_5V
- added copper zone on B.Cu, net /GND_A
- added copper zone on F.Cu, net /GND_A
- added copper zone on In1.Cu, net /GND_A
- added copper zone on In4.Cu, net /GND_A
- added copper zone on B.Cu, net /GND_C
- added copper zone on F.Cu, net /GND_C
- added copper zone on In1.Cu, net /GND_C
- added copper zone on In4.Cu, net /GND_C
- added copper zone on B.Cu, net /GND_U
- added copper zone on F.Cu, net /GND_U
- added copper zone on In1.Cu, net /GND_U
- added copper zone on In4.Cu, net /GND_U
- added copper zone on B.Cu, net /GND_W
- added copper zone on F.Cu, net /GND_W
- added copper zone on In1.Cu, net /GND_W
- added copper zone on In4.Cu, net /GND_W
- added copper zone on B.Cu, net /GND_Y
- added copper zone on F.Cu, net /GND_Y
- added copper zone on In1.Cu, net /GND_Y
- added copper zone on In4.Cu, net /GND_Y
- added copper zone on B.Cu, net /Power/GND_Z
- added copper zone on F.Cu, net /Power/GND_Z
- added copper zone on In1.Cu, net /Power/GND_Z
- added copper zone on In4.Cu, net /Power/GND_Z
- added copper zone on In2.Cu, net /Power/VIN_FUSED_Z
- added copper zone on In3.Cu, net /Power/VIN_FUSED_Z
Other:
- outline, holes or cut-outs redrawn

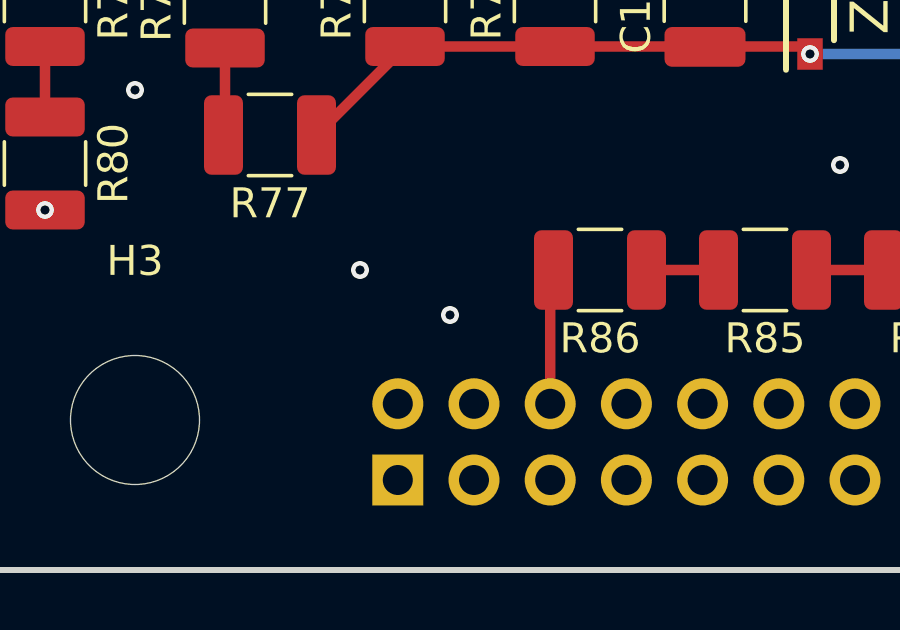
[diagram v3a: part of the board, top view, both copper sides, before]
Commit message: remove extra via
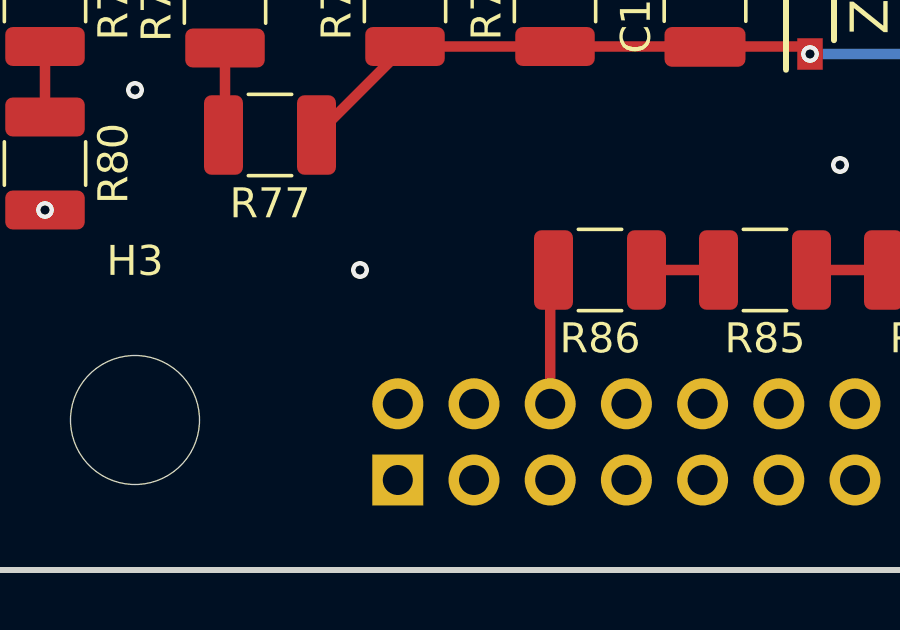
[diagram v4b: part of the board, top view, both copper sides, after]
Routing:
- net /DC_LINK_VSENSE_U: vias 2 -> 1
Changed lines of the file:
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@@
-	)
-	(via
-		(at 15.5 101.5)
-		(size 0.6)
-		(drill 0.3)
-		(layers "F.Cu" "B.Cu")
-		(net 111)
 	)
 	(via
